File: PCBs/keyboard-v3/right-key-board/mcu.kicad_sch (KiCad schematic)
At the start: 5 parts, among them J301 F31Z1A7H111008, U301 STM32G0C1CEUx

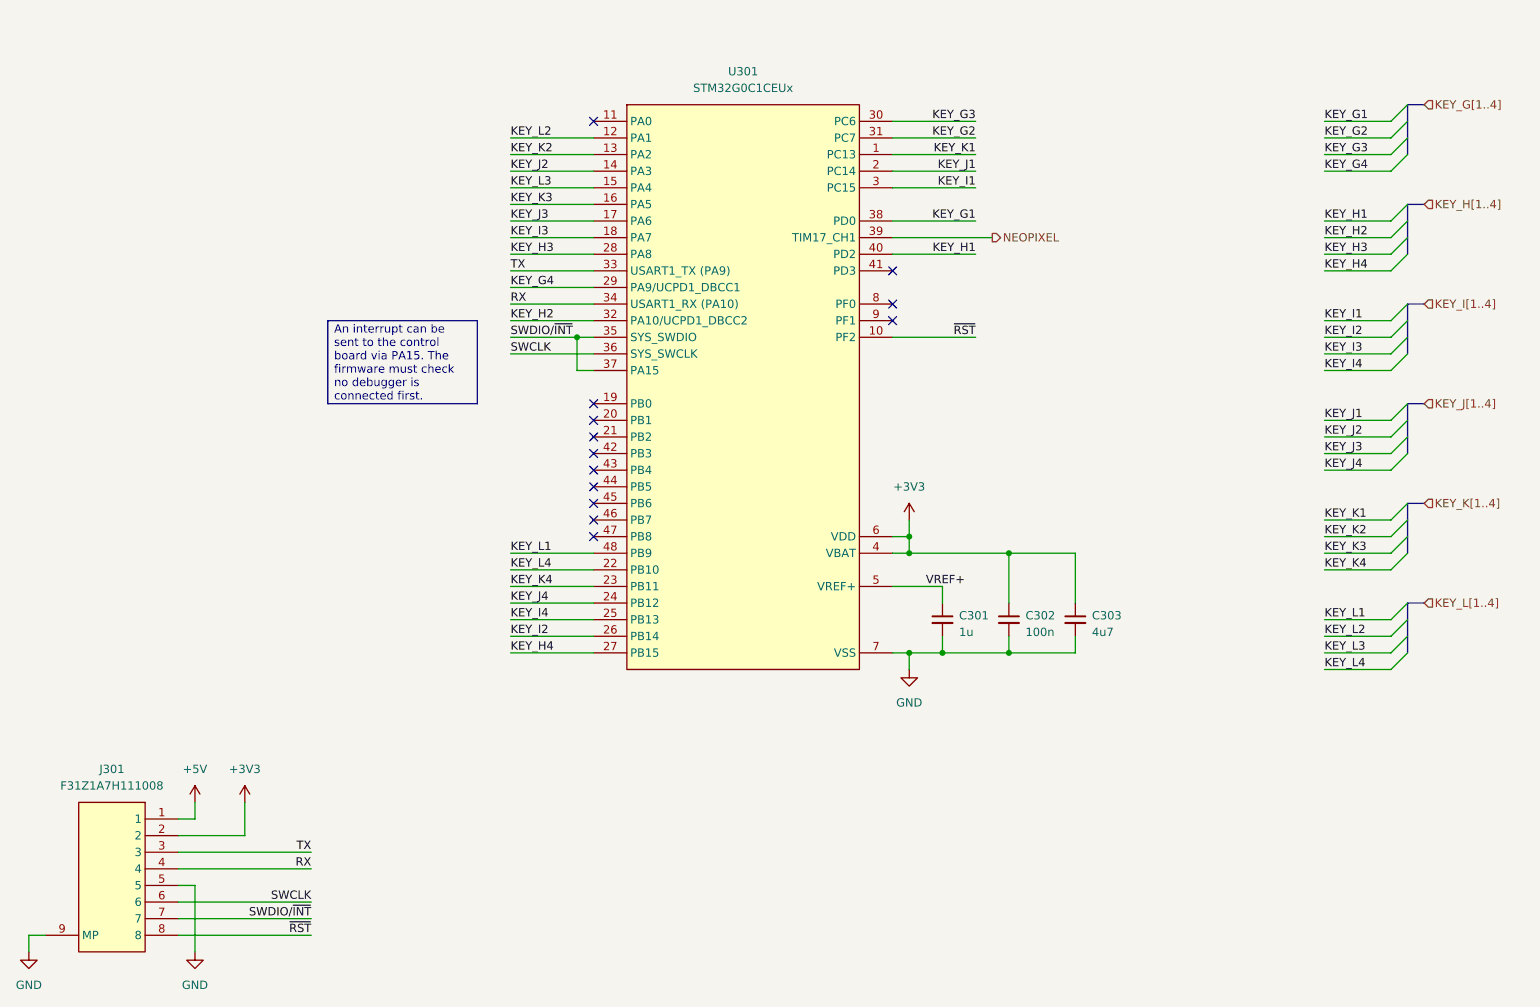
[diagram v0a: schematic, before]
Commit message: Right control board placement and schematic done
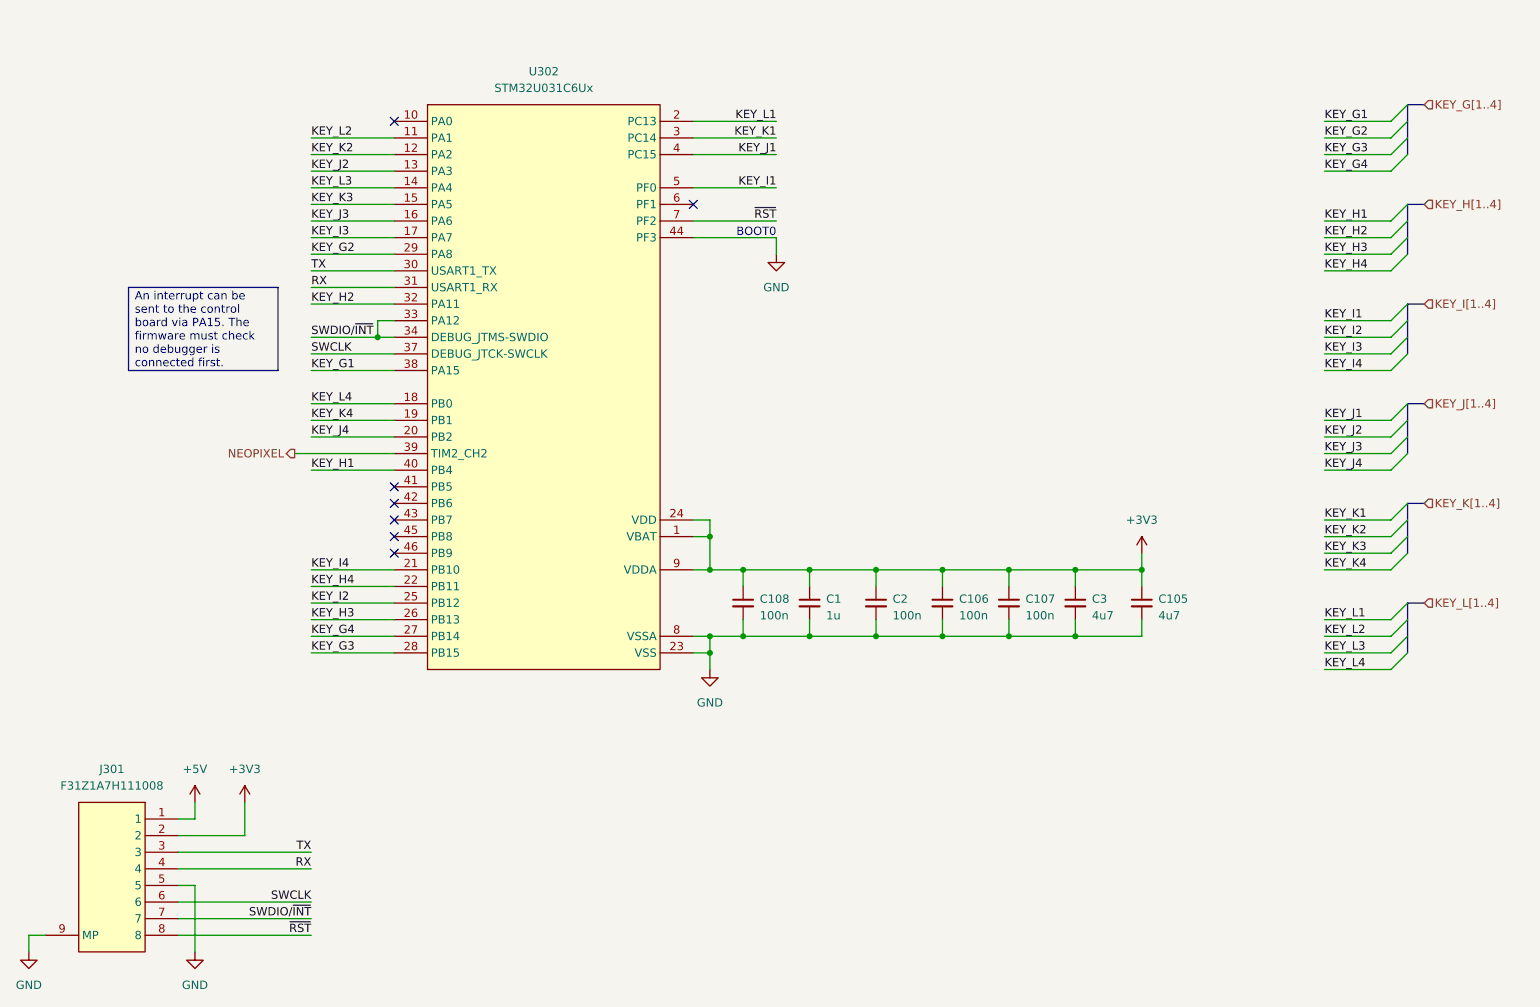
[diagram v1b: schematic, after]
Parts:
- removed U301: STM32G0C1CEUx, project_footprints:QFN50P700X700X60-49N-D, symbol STM32:STM32G0C1CEUx
- added C105: 4u7, project_footprints:C_0402, symbol DEV:C_SMALL
- added C106, C107, C108: 100n, project_footprints:C_0402, symbol DEV:C_SMALL
- added U302: STM32U031C6Ux, project_footprints:QFN50P700X700X60-49N-D, symbol STM32:STM32U031C6Ux
- renumbered C301 to C1, C302 to C2, C303 to C3
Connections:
- net VREF+ is gone; now on net +3V3: C1.1
- net +3V3: now also C105.1, C106.1, C107.1, C108.1, U302.1 (VBAT), U302.24 (VDD), U302.36 (VDD), U302.48 (VDD), U302.9 (VDDA)
- net GND: now also C105.2, C106.2, C107.2, C108.2, U302.23 (VSS), U302.35 (VSS), U302.44 (PF3), U302.47 (VSS), U302.49 (VSS), U302.8 (VSSA)
- net KEY_G1: now also U302.38 (PA15)
- net KEY_G2: now also U302.29 (PA8)
- net KEY_G3: now also U302.28 (PB15)
- net KEY_G4: now also U302.27 (PB14)
- net KEY_H1: now also U302.40 (PB4)
- net KEY_H2: now also U302.32 (PA11)
- net KEY_H3: now also U302.26 (PB13)
- net KEY_H4: now also U302.22 (PB11)
- net KEY_I1: now also U302.5 (PF0)
- net KEY_I2: now also U302.25 (PB12)
- net KEY_I3: now also U302.17 (PA7)
- net KEY_I4: now also U302.21 (PB10)
- net KEY_J1: now also U302.4 (PC15)
- net KEY_J2: now also U302.13 (PA3)
- net KEY_J3: now also U302.16 (PA6)
- net KEY_J4: now also U302.20 (PB2)
- net KEY_K1: now also U302.3 (PC14)
- net KEY_K2: now also U302.12 (PA2)
- net KEY_K3: now also U302.15 (PA5)
- net KEY_K4: now also U302.19 (PB1)
- net KEY_L1: now also U302.2 (PC13)
- net KEY_L2: now also U302.11 (PA1)
- net KEY_L3: now also U302.14 (PA4)
- net KEY_L4: now also U302.18 (PB0)
- net NEOPIXEL: now also U302.39 (PB3)
- net RX: now also U302.31 (PA10)
- net SWCLK: now also U302.37 (PA14)
- net SWDIO/~{INT}: now also U302.33 (PA12), U302.34 (PA13)
- net TX: now also U302.30 (PA9)
- net ~{RST}: now also U302.7 (PF2)
- no-connect marks 13 -> 7
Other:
- note added: "BOOT0"
- moved on the sheet: C1, C2, C3

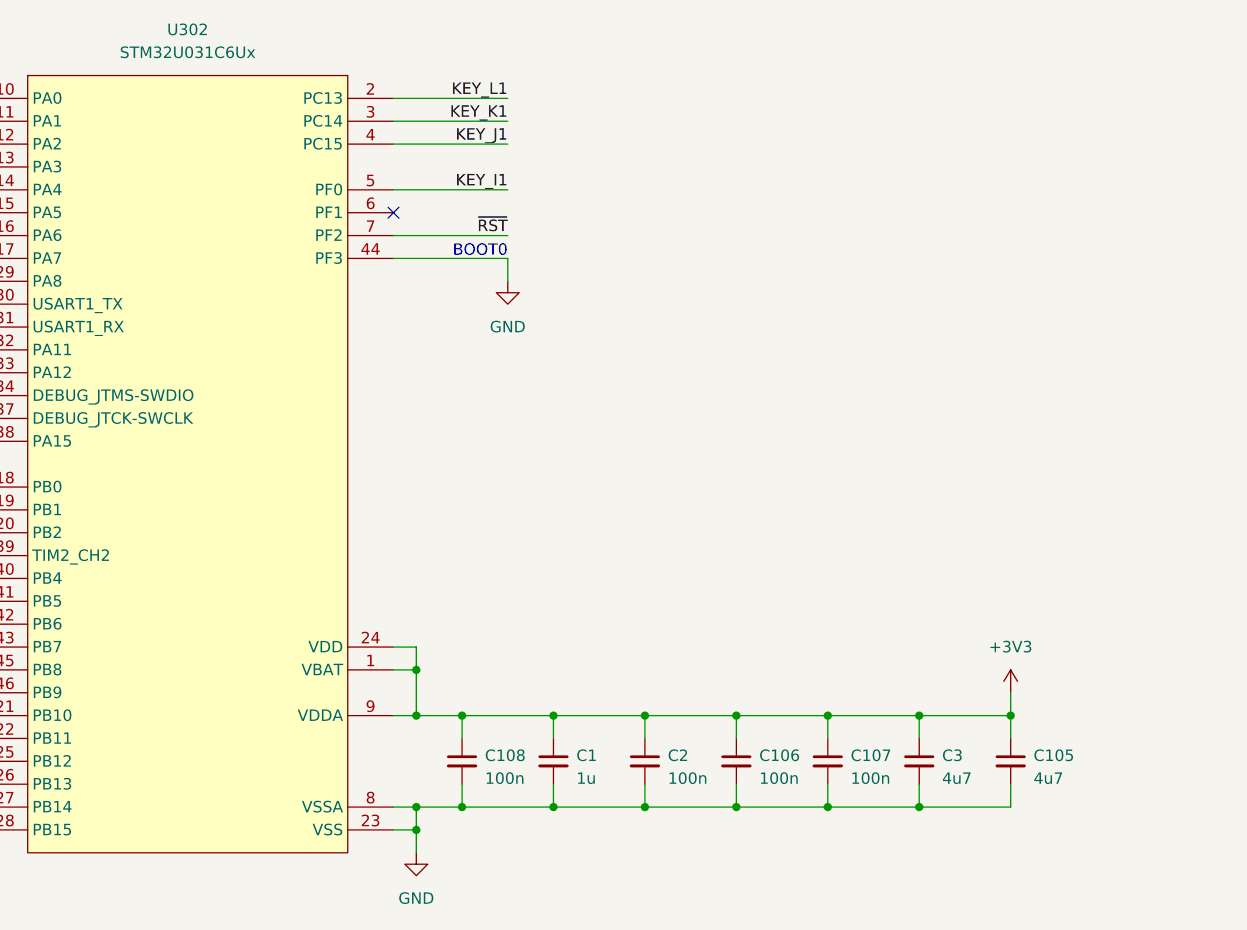
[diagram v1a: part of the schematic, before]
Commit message: Added mounting holes
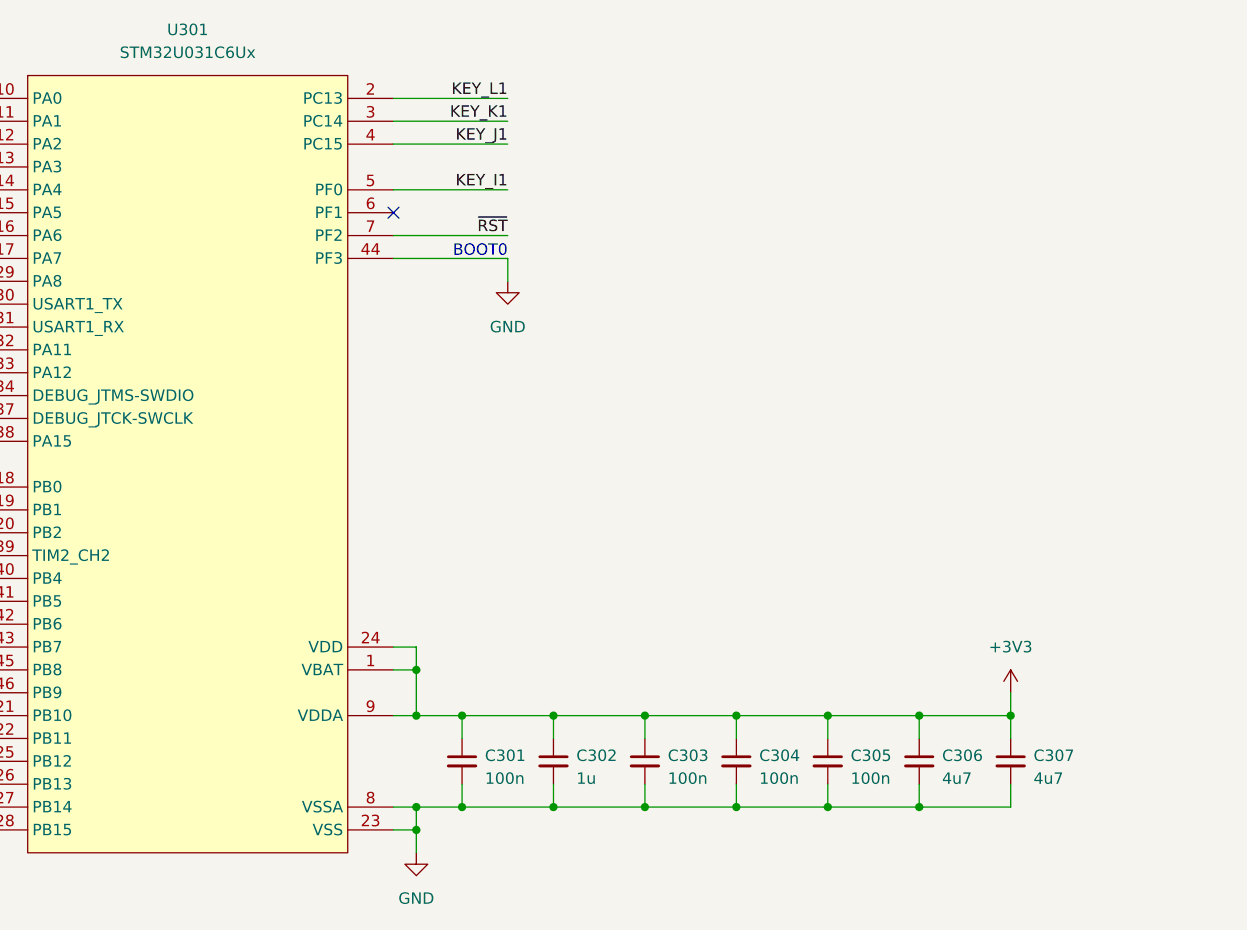
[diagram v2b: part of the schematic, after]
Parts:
- renumbered C108 to C301, C1 to C302, C2 to C303, C106 to C304, C107 to C305, C3 to C306, C105 to C307, U302 to U301
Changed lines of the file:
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@@
 		(dnp no)
 		(fields_autoplaced yes)
-		(property "Reference" "#PWR010"
+		(property "Reference" "#PWR0302"
 			(at 213.36 123.19 0)
 			(effects
@@
 			(project "right-key-board"
 				(path "/b3650411-80d8-4885-8b8e-9727427c52f9/275c43c9-42fc-40f0-aa9b-a98c3850219b"
-					(reference "#PWR010")
+					(reference "#PWR0302")
 					(unit 1)
 				)
@@
 		(on_board yes)
 		(dnp no)
-		(property "Reference" "C1"
+		(property "Reference" "C302"
 			(at 165.1 126.3713 0)
 			(effects
@@
 			(project "right-key-board"
 				(path "/b3650411-80d8-4885-8b8e-9727427c52f9/275c43c9-42fc-40f0-aa9b-a98c3850219b"
-					(reference "C1")
+					(reference "C302")
 					(unit 1)
 				)
@@
 		(on_board yes)
 		(dnp no)
-		(property "Reference" "C2"
+		(property "Reference" "C303"
 			(at 175.26 126.3713 0)
 			(effects
@@
 			(project "right-key-board"
 				(path "/b3650411-80d8-4885-8b8e-9727427c52f9/275c43c9-42fc-40f0-aa9b-a98c3850219b"
-					(reference "C2")
+					(reference "C303")
 					(unit 1)
 				)
@@
 		(on_board yes)
 		(dnp no)
-		(property "Reference" "C107"
+		(property "Reference" "C305"
 			(at 195.58 126.3713 0)
 			(effects
@@
 			(project "right-key-board"
 				(path "/b3650411-80d8-4885-8b8e-9727427c52f9/275c43c9-42fc-40f0-aa9b-a98c3850219b"
-					(reference "C107")
+					(reference "C305")
 					(unit 1)
 				)
@@
 		(dnp no)
 		(fields_autoplaced yes)
-		(property "Reference" "#PWR011"
+		(property "Reference" "#PWR0303"
 			(at 147.32 143.51 0)
 			(effects
@@
 			(project "right-key-board"
 				(path "/b3650411-80d8-4885-8b8e-9727427c52f9/275c43c9-42fc-40f0-aa9b-a98c3850219b"
-					(reference "#PWR011")
+					(reference "#PWR0303")
 					(unit 1)
 				)
@@
 		(dnp no)
 		(fields_autoplaced yes)
-		(property "Reference" "#PWR0304"
+		(property "Reference" "#PWR0305"
 			(at 76.2 161.29 0)
 			(effects
@@
 			(project ""
 				(path "/b3650411-80d8-4885-8b8e-9727427c52f9/275c43c9-42fc-40f0-aa9b-a98c3850219b"
-					(reference "#PWR0304")
+					(reference "#PWR0305")
 					(unit 1)
 				)
@@
 		(on_board yes)
 		(dnp no)
-		(property "Reference" "C3"
+		(property "Reference" "C306"
 			(at 205.74 126.3713 0)
 			(effects
@@
 			(project "right-key-board"
 				(path "/b3650411-80d8-4885-8b8e-9727427c52f9/275c43c9-42fc-40f0-aa9b-a98c3850219b"
-					(reference "C3")
+					(reference "C306")
 					(unit 1)
 				)
@@
 		(dnp no)
 		(fields_autoplaced yes)
-		(property "Reference" "U302"
+		(property "Reference" "U301"
 			(at 121.92 45.72 0)
 			(effects
@@
 			(project ""
 				(path "/b3650411-80d8-4885-8b8e-9727427c52f9/275c43c9-42fc-40f0-aa9b-a98c3850219b"
-					(reference "U302")
+					(reference "U301")
 					(unit 1)
 				)
@@
 		(on_board yes)
 		(dnp no)
-		(property "Reference" "C106"
+		(property "Reference" "C304"
 			(at 185.42 126.3713 0)
 			(effects
@@
 			(project "right-key-board"
 				(path "/b3650411-80d8-4885-8b8e-9727427c52f9/275c43c9-42fc-40f0-aa9b-a98c3850219b"
-					(reference "C106")
+					(reference "C304")
 					(unit 1)
 				)
@@
 		(dnp no)
 		(fields_autoplaced yes)
-		(property "Reference" "#PWR0303"
+		(property "Reference" "#PWR0307"
 			(at 68.58 186.69 0)
 			(effects
@@
 			(project "right-key-board"
 				(path "/b3650411-80d8-4885-8b8e-9727427c52f9/275c43c9-42fc-40f0-aa9b-a98c3850219b"
-					(reference "#PWR0303")
+					(reference "#PWR0307")
 					(unit 1)
 				)
@@
 		(dnp no)
 		(fields_autoplaced yes)
-		(property "Reference" "#PWR0302"
+		(property "Reference" "#PWR0304"
 			(at 68.58 161.29 0)
 			(effects
@@
 			(project ""
 				(path "/b3650411-80d8-4885-8b8e-9727427c52f9/275c43c9-42fc-40f0-aa9b-a98c3850219b"
-					(reference "#PWR0302")
+					(reference "#PWR0304")
 					(unit 1)
 				)
@@
 		(dnp no)
 		(fields_autoplaced yes)
-		(property "Reference" "#PWR0120"
+		(property "Reference" "#PWR0301"
 			(at 157.48 80.01 0)
 			(effects
@@
 			(project "right-key-board"
 				(path "/b3650411-80d8-4885-8b8e-9727427c52f9/275c43c9-42fc-40f0-aa9b-a98c3850219b"
-					(reference "#PWR0120")
+					(reference "#PWR0301")
 					(unit 1)
 				)
@@
 		(on_board yes)
 		(dnp no)
-		(property "Reference" "C108"
+		(property "Reference" "C301"
 			(at 154.94 126.3713 0)
 			(effects
@@
 			(project "right-key-board"
 				(path "/b3650411-80d8-4885-8b8e-9727427c52f9/275c43c9-42fc-40f0-aa9b-a98c3850219b"
-					(reference "C108")
+					(reference "C301")
 					(unit 1)
 				)
@@
 		(dnp no)
 		(fields_autoplaced yes)
-		(property "Reference" "#PWR0301"
+		(property "Reference" "#PWR0306"
 			(at 43.18 186.69 0)
 			(effects
@@
 			(project "right-key-board"
 				(path "/b3650411-80d8-4885-8b8e-9727427c52f9/275c43c9-42fc-40f0-aa9b-a98c3850219b"
-					(reference "#PWR0301")
+					(reference "#PWR0306")
 					(unit 1)
 				)
@@
 		(on_board yes)
 		(dnp no)
-		(property "Reference" "C105"
+		(property "Reference" "C307"
 			(at 215.9 126.3713 0)
 			(effects
@@
 			(project "right-key-board"
 				(path "/b3650411-80d8-4885-8b8e-9727427c52f9/275c43c9-42fc-40f0-aa9b-a98c3850219b"
-					(reference "C105")
-					(unit 1)
-				)
+					(reference "C307")
+					(unit 1)
+				)

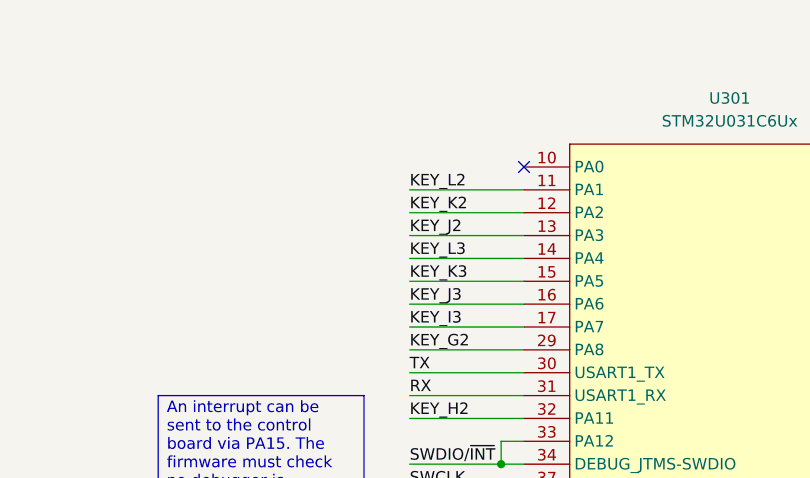
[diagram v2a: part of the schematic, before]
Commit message: Finished debug breakout board and added 5V voltage sensing to key board
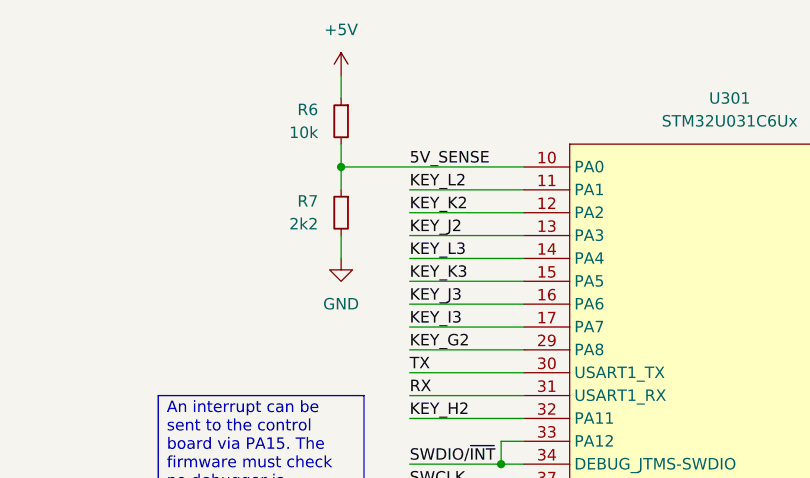
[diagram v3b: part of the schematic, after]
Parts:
- added R6: 10k, project_footprints:R_0402, symbol DEV:R_SMALL
- added R7: 2k2, project_footprints:R_0402, symbol DEV:R_SMALL
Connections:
- net +5V: now also R6.1
- net GND: now also R7.2
- net 5V_SENSE: now reaches U301.10 (PA0)
- net 5V_SENSE: now also R6.2, R7.1
- no-connect marks 7 -> 6
